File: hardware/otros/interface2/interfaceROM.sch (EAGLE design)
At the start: 15 parts, among them IC1 74HC174N, IC2 74HC32N, IC4 AM29F040S

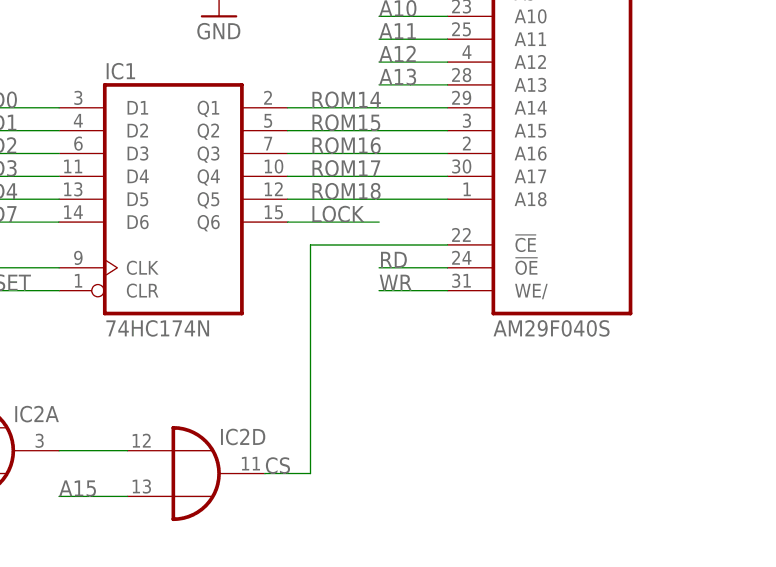
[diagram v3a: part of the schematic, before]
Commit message: Desconecto WR y lo pongo a VCC en iFrom
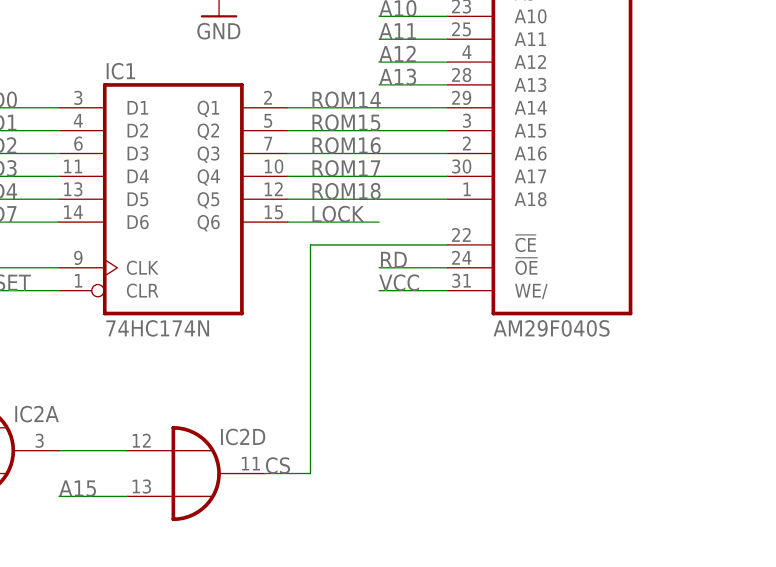
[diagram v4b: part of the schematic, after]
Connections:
- net VCC: now also IC4G$1.WE/
- net WR: no longer IC4G$1.WE/
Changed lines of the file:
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@@
 <junction x="-12.7" y="-20.32"/>
+</segment>
+<segment>
+<wire x1="116.84" y1="-20.32" x2="124.46" y2="-20.32" width="0.1524" layer="91"/>
+<label x="116.84" y="-20.32" size="1.778" layer="95"/>
+<pinref part="IC4" gate="G$1" pin="WE/"/>
 </segment>
 </net>
@@
 </segment>
 <segment>
-<wire x1="116.84" y1="-20.32" x2="124.46" y2="-20.32" width="0.1524" layer="91"/>
-<label x="116.84" y="-20.32" size="1.778" layer="95"/>
-<pinref part="IC4" gate="G$1" pin="WE/"/>
-</segment>
-<segment>
